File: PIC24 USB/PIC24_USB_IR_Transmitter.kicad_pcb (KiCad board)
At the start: 2 copper layers, 53 parts, among them CON1 USB-MINI-B, P1 CONN_6, P2 CONN_4, P3 CONN_4, P4 CONN_8, P5 CONN_4, P6 CONN_1, P7 CONN_8, P8 CONN_8X2, Q1 2N7002, Q2 MOSFET_N, Q3 MOSFET_N, Q4 MOSFET_N, Q5 MOSFET_N, Q6 MOSFET_N, Q7 MOSFET_N, Q8 MOSFET_N, U1 PIC24FJXXXGB106, U2 LM1117_SOT223_3V3, U3 50mm_5x7_Dot_Matrix_Led_Displ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, U4 MCP48X2, X1 CRYSTAL_12MHZ

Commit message: done a lot of work: ready for submission
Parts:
- removed 10u1, 10u2: C, SM1206
- added R14: 0R, SMD_Packages:SMD-1206, F.Cu at (28.5, 35.0)
- added R15: 100K, SMD_Packages:SMD-0603_r, F.Cu at (48.5, 42.2)
- added X2: 32khz, Crystals:Crystal_Round_Horizontal_3mm_BigPad, F.Cu at (64.7, 45.9)
- C5, C6: value 100n -> ?
- D1: value POWER_LED -> LED_POWER
- P6: footprint Pin_Headers:Pin_Header_Straight_1x01 -> Symbols:Symbol_OSHW-Logo_CopperTop
- moved P6 58.1 mm to (86.7, 17.8)
- moved P3 57.8 mm to (40.8, 55.2)
- moved R13 52.6 mm to (38.5, 48.0)
- moved P2 49.3 mm to (42.5, 16.5)
- moved P7 49.0 mm to (87.7, 38.0), turned to 270 degrees
- moved U4 48.2 mm to (42.1, 44.5), turned to 180 degrees
- moved D1 44.1 mm to (26.2, 58.8)
- moved R1 44.1 mm to (30.1, 59.2)
- moved U2 41.1 mm to (28.8, 49.8)
- moved C13 41.1 mm to (28.1, 55.8)
- moved P5 40.8 mm to (15.5, 23.2), turned to 270 degrees
- moved C1 37.3 mm to (20.6, 53.9)
- moved D3 35.9 mm to (72.8, 57.0), turned to 0 degrees
- moved C2 35.8 mm to (44.8, 44.2), turned to 270 degrees
- moved R4 34.3 mm to (67.3, 57.0)
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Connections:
- net /MCUSection/RP14 renamed /MCUSection/AN14/RP14/RB14
- net /MCUSection/RP29 renamed /MCUSection/AN15/RP29/RB15
- net Net-(U1-Pad24) renamed /MCUSection/AN11/RB11
- net Net-(U1-Pad27) renamed /MCUSection/AN12/RB12
- C5 pad 1: /VUSB -> /MCUSection/SOSCI
- C6 pad 1: GND -> /MCUSection/SOSCO
- C6 pad 2: +5V -> GND
- CON1 pad 1: +5V -> /VIN
- CON1 pad 2: D- -> /MCUSection/D-
- CON1 pad 3: D+ -> /MCUSection/D+
- D2 pad 2: Net-(D2-Pad2) -> GND
- P1 pad 1: ~MCLR~ -> Net-(P1-Pad1)
- P1 pad 2: +3.3V -> PGC
- P1 pad 3: GND -> PGD
- P1 pad 4: PGD -> GND
- P1 pad 5: PGC -> +3.3V
- P1 pad 6: Net-(P1-Pad6) -> ~MCLR~
- Q1 pad G: IR_LED -> /MCUSection/AN13/RB1
- R13 pad 1: /~LDAC~ -> /MCUSection/AN10/RB10
- R3 pad 1: /USER_LED -> /MCUSection/RF1
- U1 pad 21: Net-(U1-Pad21) -> /MCUSection/AN8/RP8/RB8
- U1 pad 22: Net-(U1-Pad22) -> /MCUSection/AN9/RP9/RB9
- U1 pad 23: Net-(U1-Pad23) -> /MCUSection/AN10/RB10
- U1 pad 28: Net-(U1-Pad28) -> /MCUSection/AN13/RB1
- U1 pad 33: Net-(U1-Pad33) -> /MCUSection/RP16/RF3
- U1 pad 34: Net-(U1-Pad34) -> /MCUSection/VBUS_SENSE
- U1 pad 35: Net-(U1-Pad35) -> +3.3V
- U1 pad 36: Net-(U1-Pad36) -> /MCUSection/D-
- U1 pad 37: Net-(U1-Pad37) -> /MCUSection/D+
- U1 pad 47: Net-(U1-Pad47) -> /MCUSection/SOSCI
- U1 pad 48: Net-(U1-Pad48) -> /MCUSection/SOSCO
- U1 pad 58: Net-(U1-Pad58) -> ~LCD_RESET~
- U1 pad 59: Net-(U1-Pad59) -> /MCUSection/RF1
- U4 pad 2: /~CS~DAC -> /MCUSection/RP16/RF3
- U4 pad 3: /SCKDAC -> /MCUSection/AN9/RP9/RB9
- U4 pad 4: /SDIDAC -> /MCUSection/AN8/RP8/RB8
- U4 pad 5: /~LDAC~ -> /MCUSection/AN10/RB10
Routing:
- net +5V: track 57.4 -> 257.3 mm, vias 0 -> 1
- net +3.3V: track 125.2 -> 224.4 mm, vias 0 -> 2
- net GND: track 73.2 -> 153.8 mm, vias 3 -> 9
- net SCL: track 38.5 -> 97.6 mm, vias 0 -> 2
- net SDA: track 45.1 -> 93.2 mm, vias 0 -> 4
- net Net-(R10-Pad2): track 2.76 -> 48.2 mm
- net /MCUSection/AN10/RB10: track 0.00 -> 42.2 mm, vias 0 -> 2
- net /MCUSection/D+: track 0.00 -> 36.1 mm
- net /MCUSection/D-: track 0.00 -> 35.7 mm
- net /MCUSection/PORTD6: track 66.7 -> 39.4 mm
- net /Dot Matrix Sheet/C2: track 74.6 -> 47.3 mm
- net /MCUSection/PORTD4: track 97.3 -> 70.9 mm
- net ~LCD_RESET~: track 0.00 -> 26.4 mm
- net /MCUSection/PORTD2: track 97.1 -> 71.4 mm
- net /MCUSection/PORTD5: track 89.9 -> 64.3 mm
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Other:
- board outline added: 101 x 47.6 mm
- net class POWER added: clearance 0.15, trace_width 0.254, via_dia 0.889, via_drill 0.635

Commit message: fixed some oopsies
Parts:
- moved C11 3.36 mm to (42.5, 30.2), turned to 270 degrees
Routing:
- net ~MCLR~: track 25.8 -> 29.0 mm
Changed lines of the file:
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@@
   (general
     (links 158)
-    (no_connects 2)
+    (no_connects 1)
     (area 13.259999 13.259999 114.375001 61.035001)
     (thickness 1.6)
     (drawings 21)
-    (tracks 819)
+    (tracks 823)
     (zones 0)
     (modules 54)
@@
   )
   (module SMD_Packages:SMD-0603_c (layer F.Cu)
-    (at 45.4 31.9 90)
-    (attr smd)
-    (fp_text reference C11 (at 0 0 180) (layer F.SilkS)
-      (effects (font (size 0.508 0.4572) (thickness 0.1143)))
-    )
-    (fp_text value 100n (at -1.651 0 180) (layer F.SilkS)
+    (at 42.5 30.2 270)
+    (attr smd)
+    (fp_text reference C11 (at 0 0 360) (layer F.SilkS)
+      (effects (font (size 0.508 0.4572) (thickness 0.1143)))
+    )
+    (fp_text value 100n (at -1.651 0 360) (layer F.SilkS)
       (effects (font (size 0.508 0.4572) (thickness 0.1143)))
     )
@@
     (fp_line (start 1.19888 -0.635) (end 1.19888 0.635) (layer F.SilkS) (width 0.11938))
     (fp_line (start -1.19888 0.635) (end -1.19888 -0.635) (layer F.SilkS) (width 0.11938))
-    (pad 1 smd rect (at -0.762 0 90) (size 0.635 1.143) (layers F.Cu F.Paste F.Mask)
-      (net 11 GND))
-    (pad 2 smd rect (at 0.762 0 90) (size 0.635 1.143) (layers F.Cu F.Paste F.Mask)
+    (pad 1 smd rect (at -0.762 0 270) (size 0.635 1.143) (layers F.Cu F.Paste F.Mask)
+      (net 11 GND))
+    (pad 2 smd rect (at 0.762 0 270) (size 0.635 1.143) (layers F.Cu F.Paste F.Mask)
       (net 16 ~MCLR~))
     (model smd\capacitors\C0603.wrl
@@
   (gr_line (start 32.135 21.2) (end 32.735 19.9) (layer F.SilkS) (width 0.2))
   (via (at 78.7 48.6) (size 0.889) (layers F.Cu B.Cu) (net 0))
+  (segment (start 38.8 32.662) (end 46.77 32.662) (width 0.254) (layer F.Cu) (net 1))
+  (segment (start 46.77 32.662) (end 47.246 33.138) (width 0.254) (layer F.Cu) (net 1))
+  (segment (start 47.246 33.138) (end 47.5 33.138) (width 0.254) (layer F.Cu) (net 1))
   (segment (start 29.81 17.5476) (end 29.81 17.7) (width 0.254) (layer F.Cu) (net 1))
   (segment (start 28.36938 16.10698) (end 29.81 17.5476) (width 0.254) (layer F.Cu) (net 1))
@@
   (segment (start 49.33566 37.35184) (end 49.8515 37.35184) (width 0.254) (layer F.Cu) (net 1))
   (segment (start 49.8515 37.35184) (end 50.8675 37.35184) (width 0.254) (layer F.Cu) (net 1))
-  (segment (start 38.8 32.662) (end 39.6255 32.662) (width 0.254) (layer F.Cu) (net 1))
-  (segment (start 39.6255 32.662) (end 40.673 33.7095) (width 0.254) (layer F.Cu) (net 1))
-  (segment (start 40.673 33.7095) (end 46.6745 33.7095) (width 0.254) (layer F.Cu) (net 1))
-  (segment (start 46.6745 33.7095) (end 47.246 33.138) (width 0.254) (layer F.Cu) (net 1))
-  (segment (start 47.246 33.138) (end 47.5 33.138) (width 0.254) (layer F.Cu) (net 1))
   (segment (start 50.8675 33.85172) (end 47.64222 33.85172) (width 0.254) (layer F.Cu) (net 1))
   (segment (start 47.64222 33.85172) (end 47.5 33.7095) (width 0.254) (layer F.Cu) (net 1))
@@
   (via (at 54.70976 38.553596) (size 0.889) (drill 0.635) (layers F.Cu B.Cu) (net 15))
   (segment (start 50.8675 39.8512) (end 50.236115 39.8512) (width 0.15) (layer F.Cu) (net 15))
+  (segment (start 42.5 30.962) (end 42.438 30.9) (width 0.15) (layer F.Cu) (net 16))
+  (segment (start 42.438 30.9) (end 42.4 30.9) (width 0.15) (layer F.Cu) (net 16))
+  (segment (start 42.4 30.9) (end 42.5 31) (width 0.15) (layer F.Cu) (net 16))
+  (segment (start 42.5 31) (end 45.44451 31) (width 0.15) (layer F.Cu) (net 16))
+  (segment (start 45.538 31) (end 45.44451 31) (width 0.15) (layer F.Cu) (net 16))
+  (segment (start 45.44451 31) (end 38.938 31) (width 0.15) (layer F.Cu) (net 16))
+  (segment (start 45.738 28.8) (end 45.738 30.8) (width 0.15) (layer F.Cu) (net 16))
+  (segment (start 45.738 30.8) (end 45.538 31) (width 0.15) (layer F.Cu) (net 16))
+  (segment (start 38.938 31) (end 38.8 31.138) (width 0.15) (layer F.Cu) (net 16))
   (segment (start 38.8 31.138) (end 38.8 23.1364) (width 0.15) (layer F.Cu) (net 16))
   (segment (start 38.8 23.1364) (end 33.3636 17.7) (width 0.15) (layer F.Cu) (net 16))
   (segment (start 33.3636 17.7) (end 32.35 17.7) (width 0.15) (layer F.Cu) (net 16))
-  (segment (start 45.738 30.8) (end 45.4 31.138) (width 0.15) (layer F.Cu) (net 16))
-  (segment (start 45.738 28.8) (end 45.738 30.8) (width 0.15) (layer F.Cu) (net 16))
-  (segment (start 45.4 31.138) (end 38.8 31.138) (width 0.15) (layer F.Cu) (net 16))
   (segment (start 53.938 55.5) (end 53.938 53.937) (width 0.15) (layer F.Cu) (net 17))
   (segment (start 53.938 53.937) (end 54.50055 53.37445) (width 0.15) (layer F.Cu) (net 17))

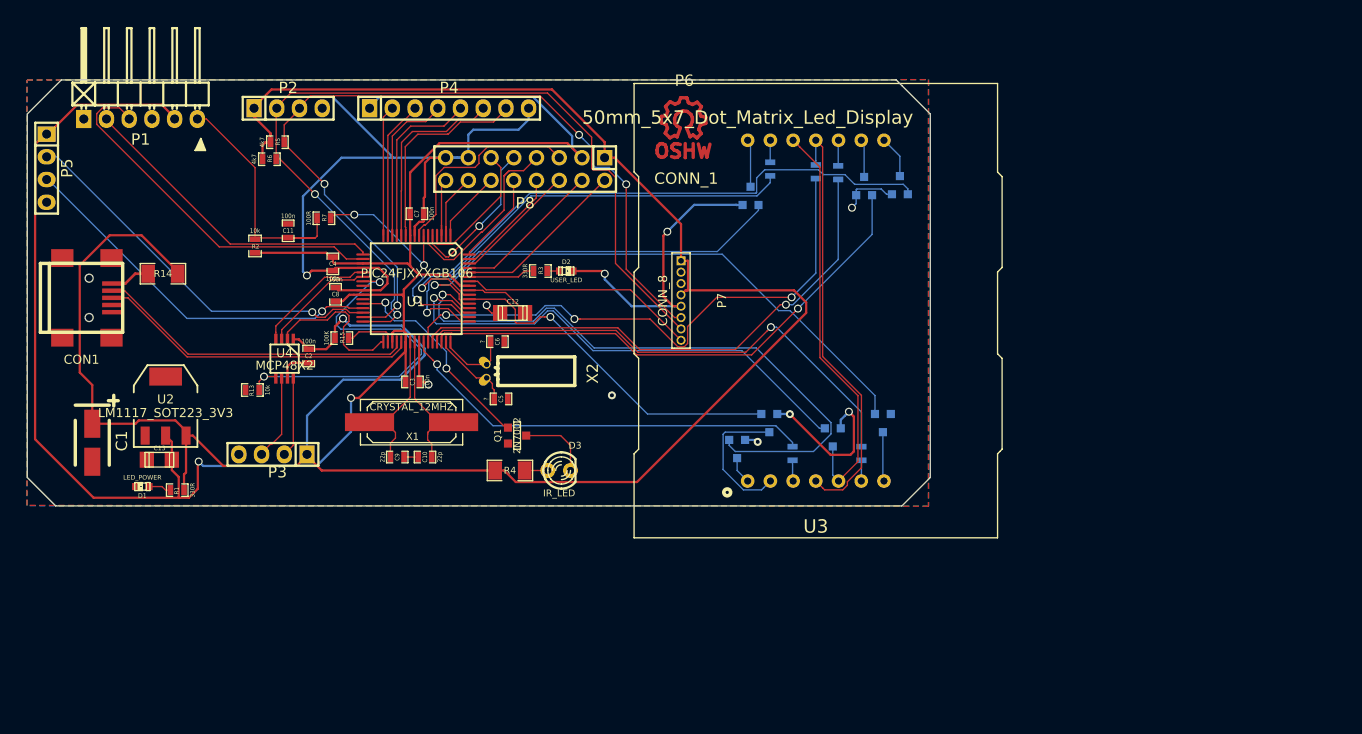
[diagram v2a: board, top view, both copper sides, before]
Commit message: shrinked, added temp sensor, updated gerbers and submitted them
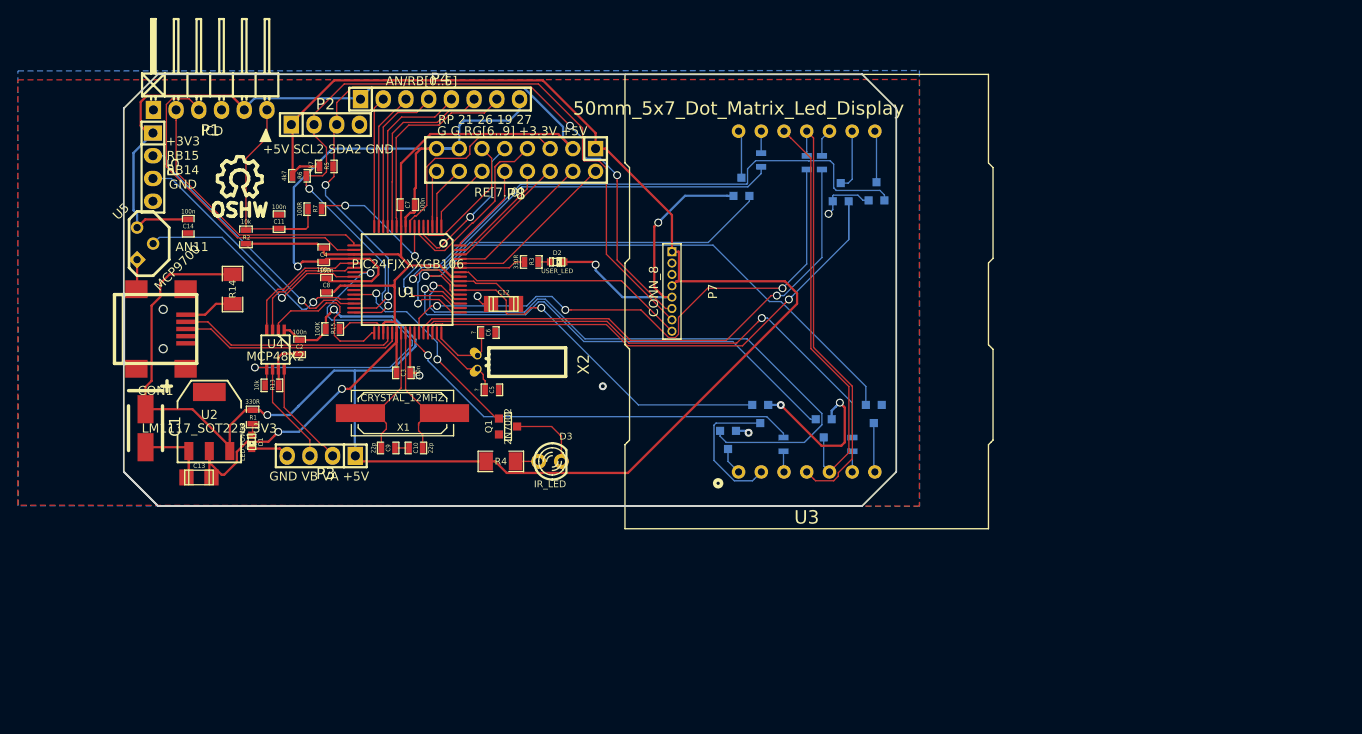
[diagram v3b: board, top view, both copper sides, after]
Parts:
- added C14: 100n, SMD_Packages:SMD-0603_c, F.Cu at (31.3, 29.7)
- added U5: MCP9700, Discret:TO92-123, F.Cu at (25.6, 31.6)
- P6: footprint Symbols:Symbol_OSHW-Logo_CopperTop -> Symbols:Symbol_OSHW-Logo_SilkScreen
- Q2, Q3, Q4, Q5, Q6, Q7, Q8: value MOSFET_N -> 2N7002
- moved P6 50.1 mm to (37.1, 24.4)
- moved D1 13.2 mm to (38.4, 53.8), turned to 270 degrees
- moved P5 11.9 mm to (27.4, 23.1)
- moved R1 11.7 mm to (38.5, 51.0), turned to 270 degrees
- moved CON1 8.99 mm to (27.7, 41.2)
- moved R14 7.97 mm to (36.3, 36.7), turned to 270 degrees
- moved P1 7.85 mm to (33.8, 16.7)
- moved C1 6.17 mm to (26.6, 52.3)
- moved R5 6.10 mm to (46.8, 23.0)
- moved P3 5.40 mm to (46.2, 55.4)
- moved U2 5.18 mm to (33.7, 51.5)
- moved C13 4.85 mm to (32.5, 57.8)
- moved P2 4.55 mm to (46.7, 18.3)
- moved R6 3.84 mm to (43.8, 24.1)
- moved Q2 2.70 mm to (104.3, 25.9)
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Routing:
- net +3.3V: track 223.9 -> 190.8 mm
- net /MCUSection/AN11/RB11: track 0.00 -> 26.9 mm, vias 0 -> 1
- net +5V: track 257.3 -> 235.5 mm, vias 1 -> 2
- net /MCUSection/AN14/RP14/RB14: track 42.4 -> 29.2 mm
- net /MCUSection/AN15/RP29/RB15: track 43.3 -> 30.7 mm
- net /MCUSection/D+: track 36.1 -> 25.1 mm
- net /MCUSection/D-: track 35.7 -> 24.7 mm
- net GND: track 153.8 -> 164.5 mm
- net SDA: track 93.2 -> 85.2 mm
- net PGD: track 42.3 -> 36.9 mm
- net SCL: track 97.6 -> 92.3 mm
- net PGC: track 35.5 -> 30.8 mm
- net /VOUTA: track 8.96 -> 12.1 mm
- net Net-(Q2-PadD): track 4.24 -> 7.28 mm
- net /MCUSection/PORTD0: track 59.9 -> 62.4 mm
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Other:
- board size 101 x 47.6 mm -> 86.4 x 48.3 mm
- board text added: "+3V3 RB15 RB14 GND"
- board text added: "+5V SCL2 SDA2 GND"
- board text added: "AN/RB[0..5]"
- board text added: "AN11"
- board text added: "G G RG[6..9] +3.3V +5V"
- board text added: "GND VB VA +5V"
- board text added: "ICD"
- board text added: "RE[7..0]"
- board text added: "RP 21 26 19 27"

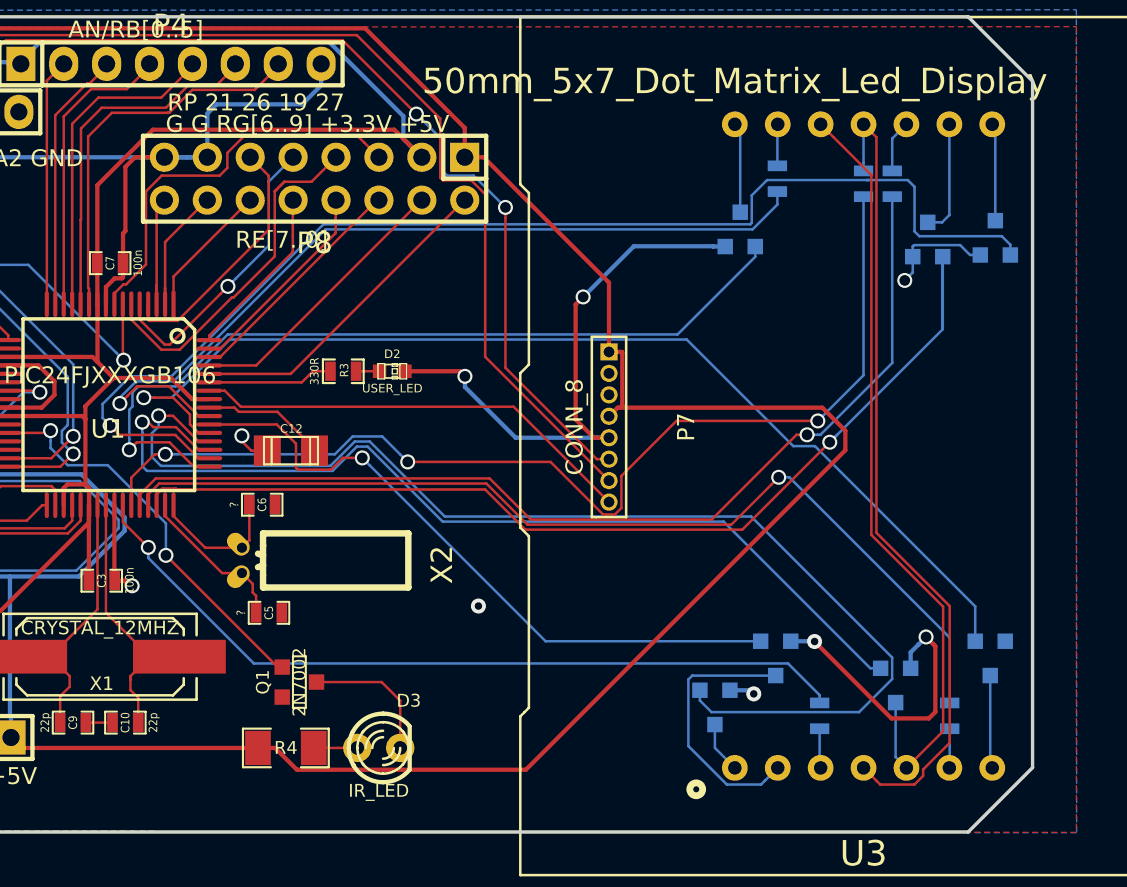
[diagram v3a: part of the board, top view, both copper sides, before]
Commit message: changed wrong polarity of led matrix in schematic, started correcting the layout
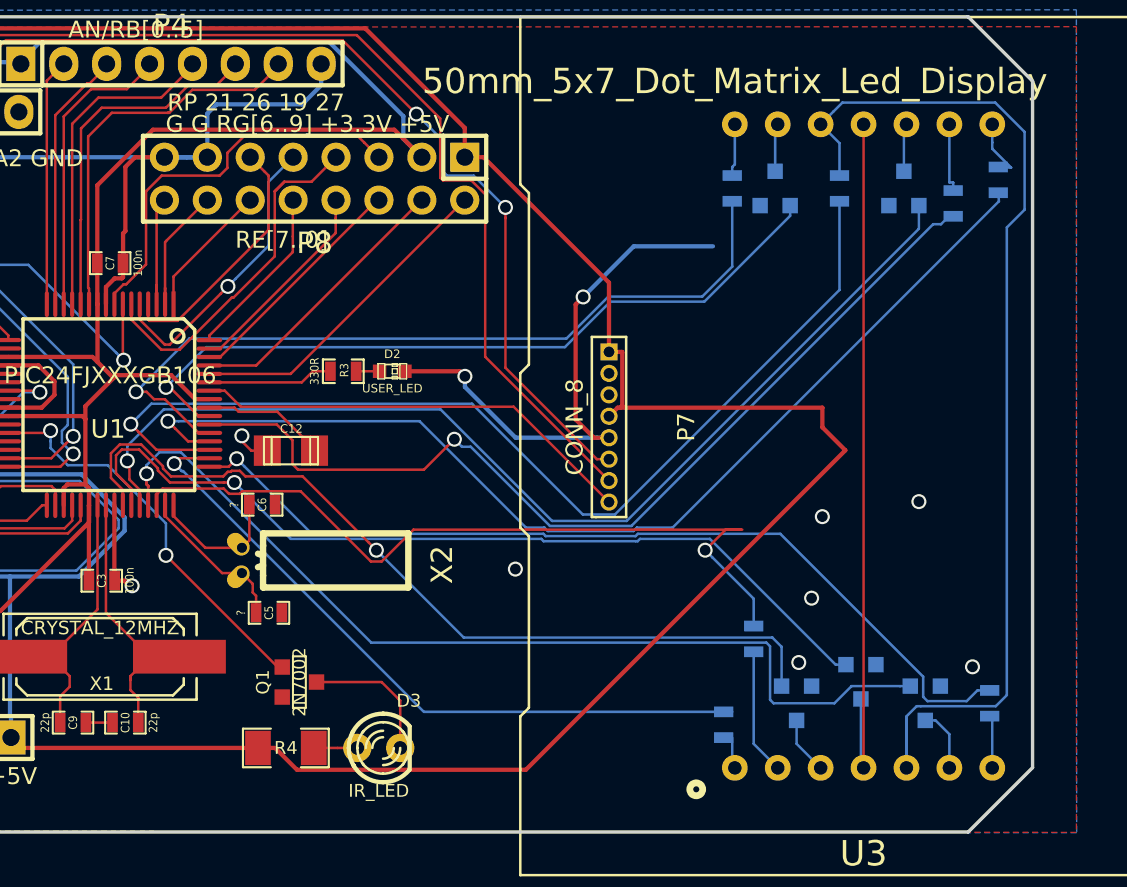
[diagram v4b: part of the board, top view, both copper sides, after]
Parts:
- removed Q7, Q8: 2N7002, SMD_Packages:SOT-23-GDS
- added R16: 330R, SMD_Packages:SMD-0603_r, B.Cu at (92.7, 22.9)
- added R17: 330R, SMD_Packages:SMD-0603_r, B.Cu at (105.8, 23.7)
- moved R10 33.1 mm to (92.2, 54.6)
- moved R12 31.9 mm to (108.5, 22.4)
- moved Q5 29.4 mm to (102.9, 22.9), turned to 0 degrees
- moved Q3 28.3 mm to (96.5, 53.3), turned to 180 degrees
- moved Q4 27.5 mm to (100.3, 52.1), turned to 180 degrees
- moved R8 27.3 mm to (94.0, 49.5)
- moved Q6 12.5 mm to (104.1, 53.3)
- moved R9 10.1 mm to (108.0, 53.3), turned to 90 degrees
- moved Q2 9.53 mm to (95.2, 22.9)
- moved R11 3.14 mm to (99.1, 22.9), turned to 270 degrees
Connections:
- CON1 pad 4: Net-(CON1-Pad4) -> (no net)
- P1 pad 1: Net-(P1-Pad1) -> (no net)
- P7 pad 2: Net-(P7-Pad2) -> (no net)
- P7 pad 3: Net-(P7-Pad3) -> (no net)
- Q2 pad G: /MCUSection/PORTD0 -> /Dot Matrix Sheet/C1
- Q3 pad G: /MCUSection/PORTD1 -> /Dot Matrix Sheet/C2
- Q4 pad G: /MCUSection/PORTD2 -> /Dot Matrix Sheet/C3
- Q5 pad G: /MCUSection/PORTD3 -> /Dot Matrix Sheet/C4
- Q6 pad G: /MCUSection/PORTD4 -> /Dot Matrix Sheet/C5
- R10 pad 1: /Dot Matrix Sheet/C3 -> Net-(R10-Pad1)
- R10 pad 2: Net-(R10-Pad2) -> /MCUSection/PORTD2
- R11 pad 1: /Dot Matrix Sheet/C4 -> Net-(R11-Pad1)
- R11 pad 2: Net-(R11-Pad2) -> /MCUSection/PORTD3
- R12 pad 1: /Dot Matrix Sheet/C5 -> Net-(R12-Pad1)
- R12 pad 2: Net-(R12-Pad2) -> /MCUSection/PORTD4
- R8 pad 1: /Dot Matrix Sheet/C1 -> Net-(R8-Pad1)
- R8 pad 2: Net-(R8-Pad2) -> /MCUSection/PORTD0
- R9 pad 1: /Dot Matrix Sheet/C2 -> Net-(R9-Pad1)
- R9 pad 2: Net-(R9-Pad2) -> /MCUSection/PORTD1
- U1 pad 27: /MCUSection/AN12/RB12 -> (no net)
- U3 pad 1: Net-(Q6-PadD) -> Net-(R10-Pad1)
- U3 pad 10: Net-(R11-Pad2) -> Net-(Q5-PadD)
- U3 pad 12,5: Net-(Q5-PadD) -> Net-(R11-Pad1)
- U3 pad 13: Net-(R8-Pad2) -> Net-(Q2-PadD)
- U3 pad 14: Net-(Q3-PadD) -> Net-(R16-Pad1)
- U3 pad 2: Net-(Q8-PadD) -> Net-(R8-Pad1)
- U3 pad 3: Net-(R9-Pad2) -> Net-(Q3-PadD)
- U3 pad 4,11: Net-(R10-Pad2) -> Net-(Q4-PadD)
- U3 pad 6: Net-(R12-Pad2) -> Net-(Q6-PadD)
- U3 pad 7: Net-(Q7-PadD) -> Net-(R9-Pad1)
- U3 pad 8: Net-(Q4-PadD) -> Net-(R12-Pad1)
- U3 pad 9: Net-(Q2-PadD) -> Net-(R17-Pad1)
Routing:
- net Net-(R11-Pad1): track 0.00 -> 63.1 mm
- net Net-(R10-Pad2): track 48.2 -> 0.00 mm
- net Net-(Q5-PadD): track 46.1 -> 2.84 mm
- net Net-(Q4-PadD): track 5.78 -> 42.2 mm
- net /MCUSection/PORTD2: track 72.2 -> 42.0 mm
- net GND: track 164.5 -> 138.3 mm, vias 9 -> 5
- net /MCUSection/PORTD6: track 39.4 -> 56.4 mm
- net /MCUSection/PORTD5: track 64.3 -> 47.6 mm
- net /MCUSection/PORTD0: track 62.4 -> 46.5 mm
- net Net-(Q8-PadD): track 15.9 -> 0.00 mm
- net /Dot Matrix Sheet/C3: track 63.0 -> 52.1 mm, vias 3 -> 1
- net /MCUSection/PORTD4: track 70.9 -> 63.4 mm
- net Net-(R8-Pad1): track 0.00 -> 7.46 mm
- net /Dot Matrix Sheet/C1: track 51.2 -> 45.7 mm
- net Net-(Q7-PadD): track 5.51 -> 0.00 mm
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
